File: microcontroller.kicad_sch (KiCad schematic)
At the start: 1 part

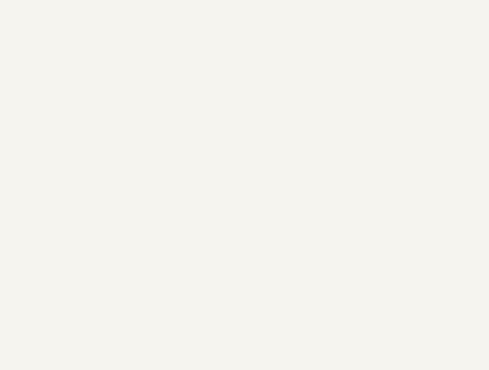
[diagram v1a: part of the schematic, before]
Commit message: added switches
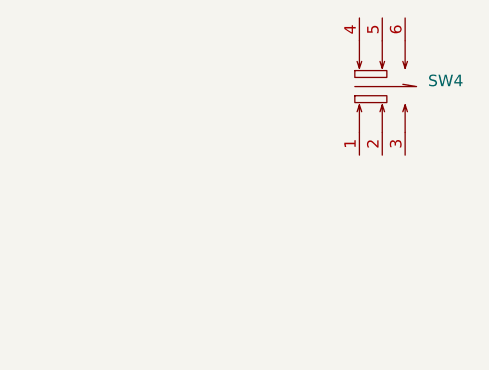
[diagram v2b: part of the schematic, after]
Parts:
- added SW4: ~, Custom_Parts:Switch_XKB5858, symbol Custom_Parts:Switch_XKB5858
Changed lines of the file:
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@@
 	(paper "A4")
+	(symbol
+		(lib_id "Custom_Parts:Switch_XKB5858")
+		(at 222.25 44.45 0)
+		(unit 1)
+		(exclude_from_sim no)
+		(in_bom yes)
+		(on_board yes)
+		(dnp no)
+		(fields_autoplaced yes)
+		(property "Reference" "SW4"
+			(at 227.33 43.8149 0)
+			(effects
+				(font
+					(size 1.27 1.27)
+				)
+				(justify left)
+			)
+		)
+		(property "Value" "~"
+			(at 227.33 45.72 0)
+			(effects
+				(font
+					(size 1.27 1.27)
+				)
+				(justify left)
+			)
+		)
+		(property "Footprint" "Custom_Parts:Switch_XKB5858"
+			(at 222.25 44.45 0)
+			(effects
+				(font
+					(size 1.27 1.27)
+				)
+				(hide yes)
+			)
+		)
+		(property "Datasheet" "https://item.szlcsc.com/datasheet/XKB5858-W-TP-75/724371.html"
+			(at 222.25 44.45 0)
+			(effects
+				(font
+					(size 1.27 1.27)
+				)
+				(hide yes)
+			)
+		)
+		(property "Description" "Self Lock / No Lock:Non-Latching Actuator Style:Square Button Mounting Type:Surface Mount,Vertical Contact Current:100mA Voltage Rating:30V Actuator/Cap Color:White With Lamp:Without Termination Style:SMD(SMT) Tab Operating Force:1.6N Operating Temperatur"
+			(at 222.25 44.45 0)
+			(effects
+				(font
+					(size 1.27 1.27)
+				)
+				(hide yes)
+			)
+		)
+		(property "Manufacturer Part" "XKB5858-W-TP-75"
+			(at 222.25 44.45 0)
+			(effects
+				(font
+					(size 1.27 1.27)
+				)
+				(hide yes)
+			)
+		)
+		(property "Manufacturer" "XKB Connection(中国星坤)"
+			(at 222.25 44.45 0)
+			(effects
+				(font
+					(size 1.27 1.27)
+				)
+				(hide yes)
+			)
+		)
+		(property "Supplier Part" "C692488"
+			(at 222.25 44.45 0)
+			(effects
+				(font
+					(size 1.27 1.27)
+				)
+				(hide yes)
+			)
+		)
+		(property "Supplier" "LCSC"
+			(at 222.25 44.45 0)
+			(effects
+				(font
+					(size 1.27 1.27)
+				)
+				(hide yes)
+			)
+		)
+		(property "LCSC Part Name" "按键开关5.8*按键开关5.8贴片无锁开关 平头"
+			(at 222.25 44.45 0)
+			(effects
+				(font
+					(size 1.27 1.27)
+				)
+				(hide yes)
+			)
+		)
+		(property "LCSC" "C692488"
+			(at 222.25 44.45 0)
+			(effects
+				(font
+					(size 1.27 1.27)
+				)
+				(hide yes)
+			)
+		)
+		(pin "5"
+		)
+		(pin "1"
+		)
+		(pin "6"
+		)
+		(pin "4"
+		)
+		(pin "2"
+		)
+		(pin "3"
+		)
+		(instances
+			(project "mt-rt"
+				(path "/ee47f507-02e8-4ef5-a6d4-1ac4b2022b93/d98c736e-7552-409d-af25-f5fe8dce0887"
+					(reference "SW4")
+					(unit 1)
+				)
+			)
+		)
+	)
 	(symbol
 		(lib_id "MCU_ST_STM32WB:STM32WB55RGVx")

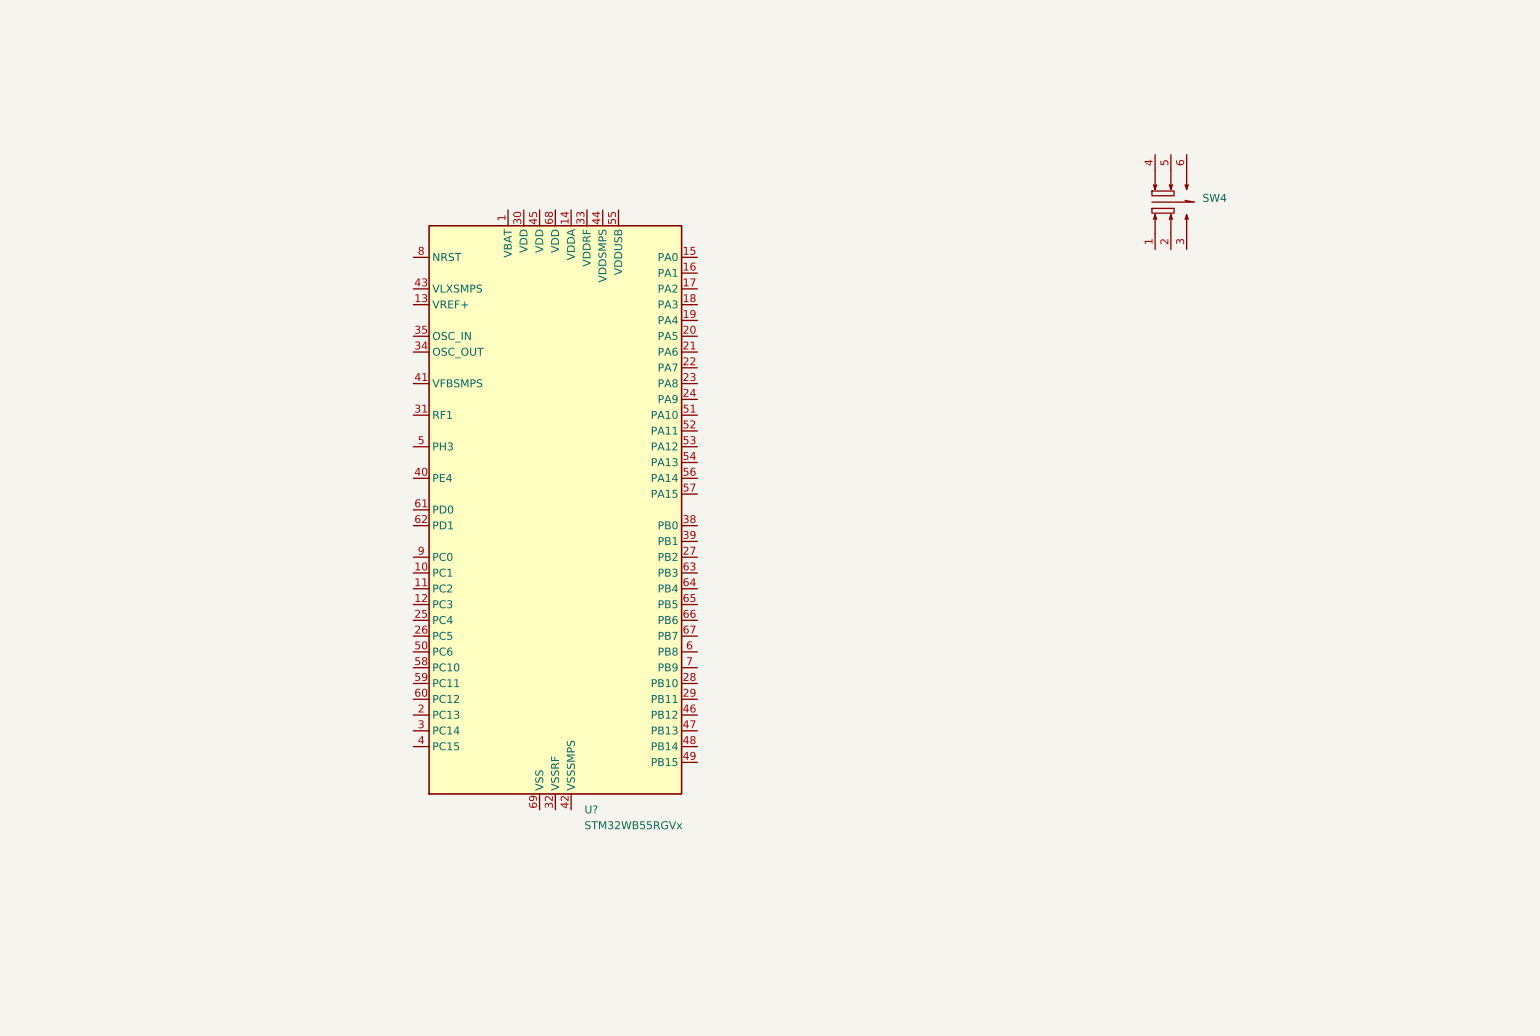
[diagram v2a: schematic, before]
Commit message: Added debug connector and mapped Boot0 and NRST
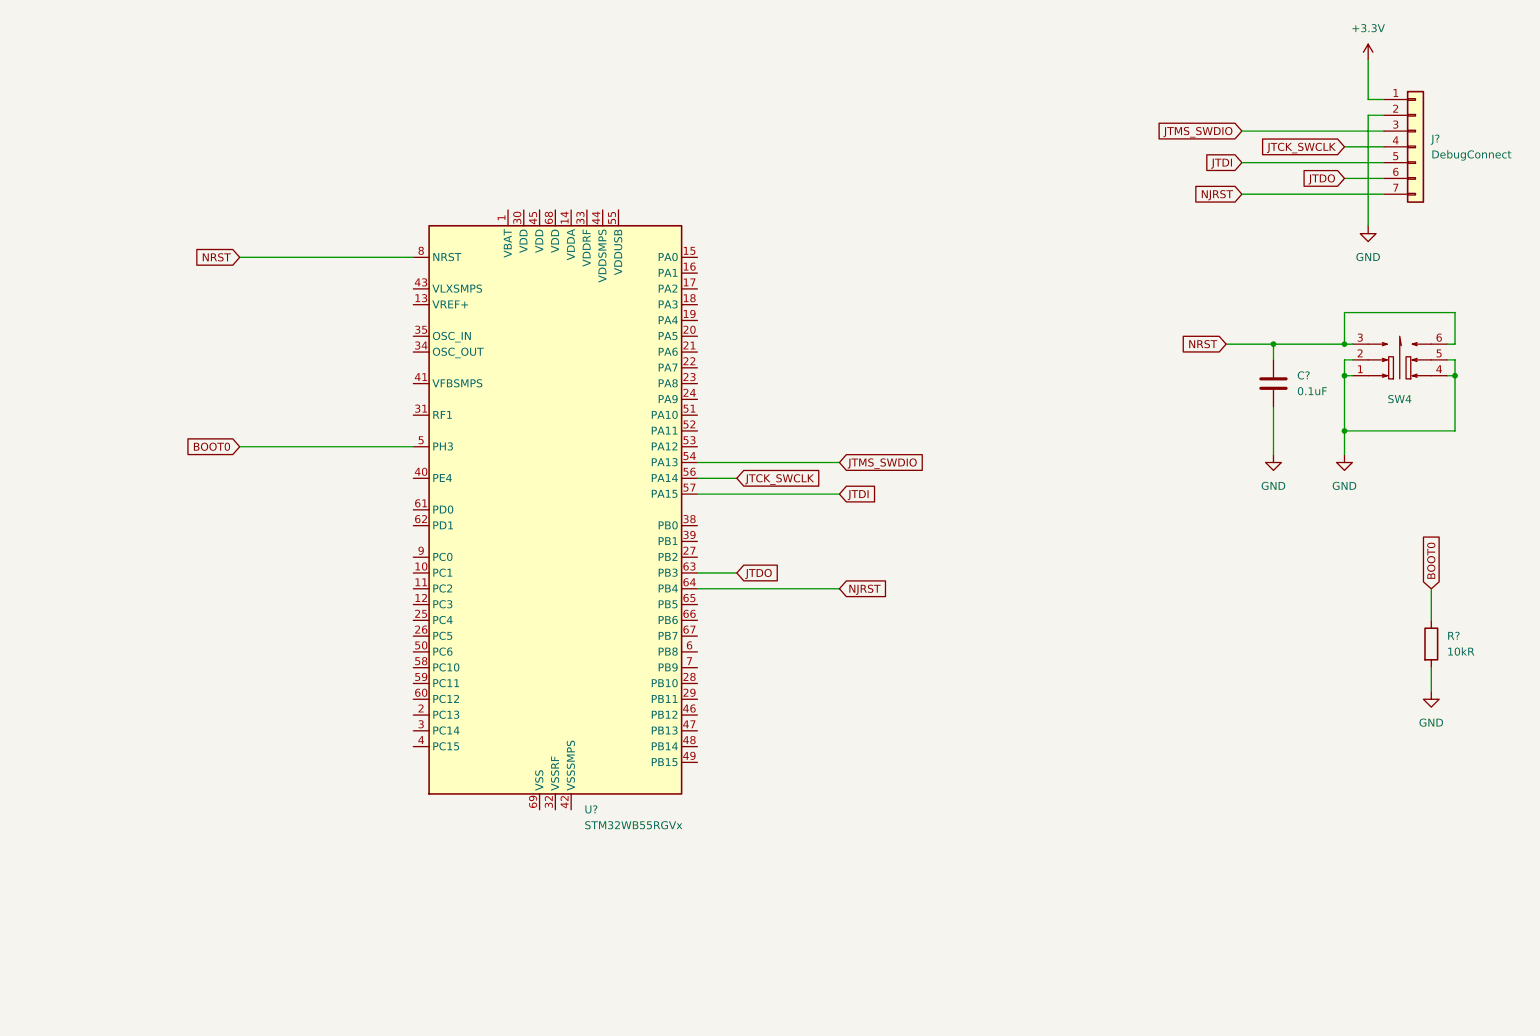
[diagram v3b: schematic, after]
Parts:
- added C?: 0.1uF, Capacitor_SMD:C_0805_2012Metric, symbol Device:C
- added J?: DebugConnect, Connector_PinHeader_2.54mm:PinHeader_1x07_P2.54mm_Vertical, symbol Connector_Generic:Conn_01x07
- added R?: 10kR, Resistor_SMD:R_0805_2012Metric, symbol Device:R
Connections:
- net GND: now reaches SW4.1
- net GND: now also SW4.2, SW4.4, SW4.5, C?.2, J?.2 (Pin_2), R?.2
- net NRST: now reaches SW4.3
- net NRST: now also SW4.6, U?.8 (NRST), C?.1
- net BOOT0: now reaches U?.5 (PH3)
- net BOOT0: now also R?.1
- net JTMS_SWDIO: now reaches U?.54 (PA13)
- net JTMS_SWDIO: now also J?.3 (Pin_3)
- net JTCK_SWCLK: now reaches U?.56 (PA14)
- net JTCK_SWCLK: now also J?.4 (Pin_4)
- net JTDI: now reaches U?.57 (PA15)
- net JTDI: now also J?.5 (Pin_5)
- net JTDO: now reaches U?.63 (PB3)
- net JTDO: now also J?.6 (Pin_6)
- net NJRST: now reaches U?.64 (PB4)
- net NJRST: now also J?.7 (Pin_7)
- new net +3.3V: J?.1 (Pin_1)
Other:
- moved on the sheet: SW4

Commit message: added base VDD Caps added SMPS circuitry added switches MCU added C to reset switch to reduce bouncing
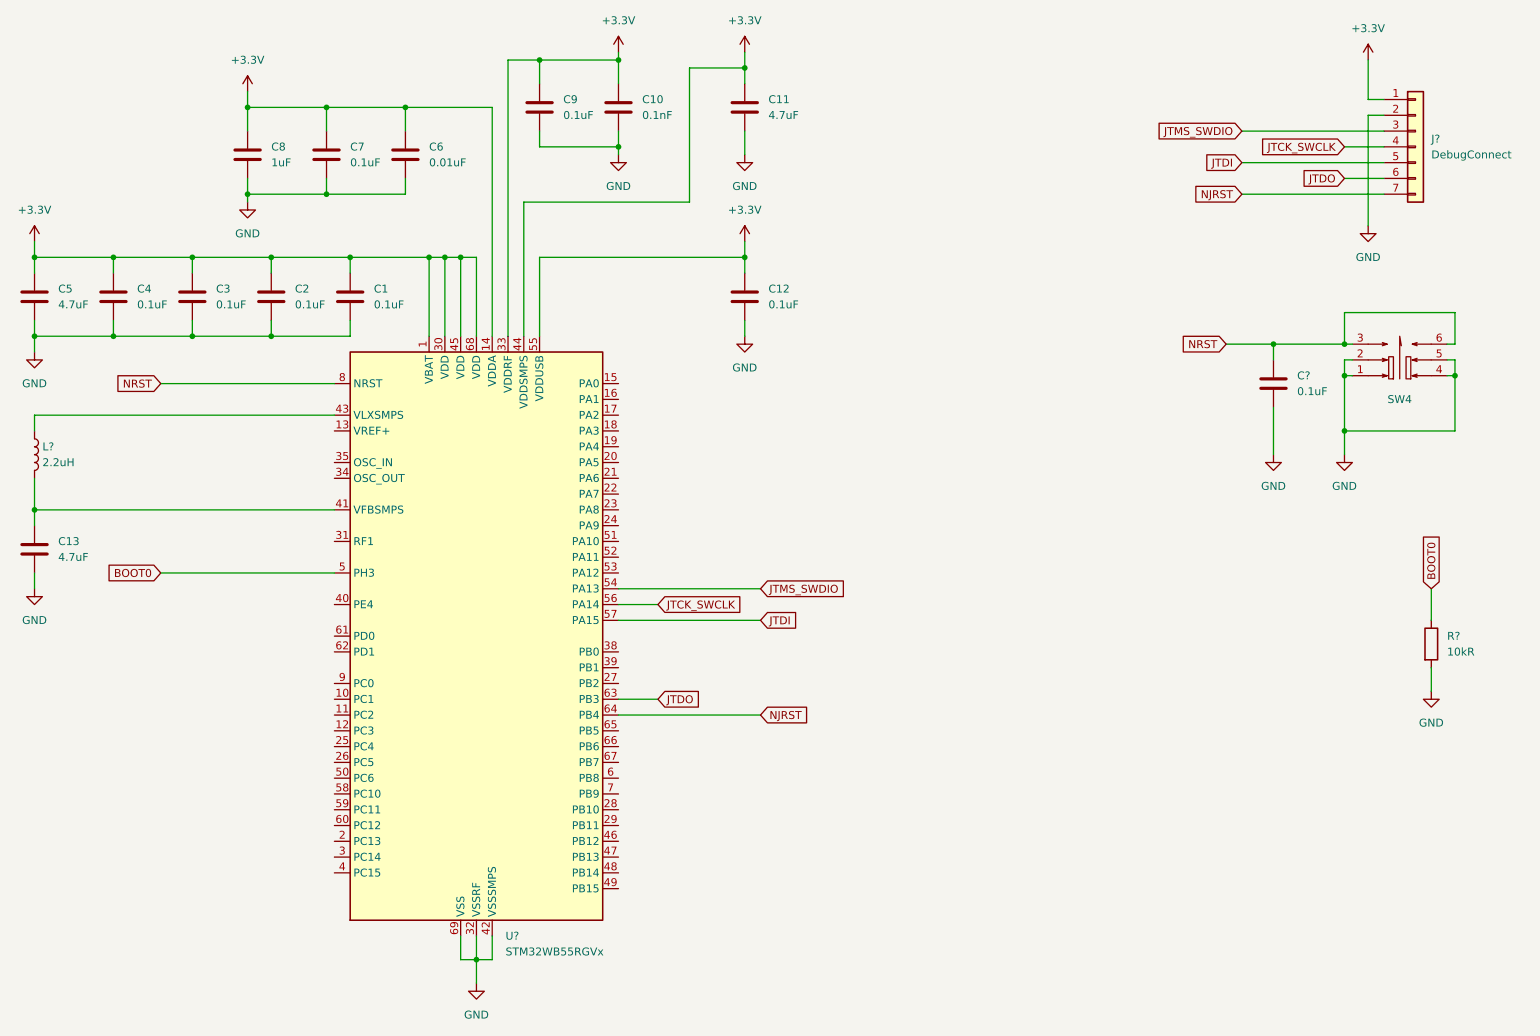
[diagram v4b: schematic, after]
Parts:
- added C1, C12, C2, C3, C4, C7, C9: 0.1uF, Capacitor_SMD:C_0805_2012Metric, symbol Device:C
- added C10: 0.1nF, Capacitor_SMD:C_0805_2012Metric, symbol Device:C
- added C11, C13, C5: 4.7uF, Capacitor_SMD:C_0805_2012Metric, symbol Device:C
- added C6: 0.01uF, Capacitor_SMD:C_0805_2012Metric, symbol Device:C
- added C8: 1uF, Capacitor_SMD:C_0805_2012Metric, symbol Device:C
- added L?: 2.2uH, symbol Device:L
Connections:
- net +3.3V: now also U?.1 (VBAT), U?.14 (VDDA), U?.30 (VDD), U?.33 (VDDRF), U?.44 (VDDSMPS), U?.45 (VDD), U?.55 (VDDUSB), U?.68 (VDD), C1.1, C10.1, C11.1, C12.1, C2.1, C3.1, C4.1, C5.1, C6.1, C7.1, C8.1, C9.1
- net GND: now also U?.32 (VSSRF), U?.42 (VSSSMPS), U?.69 (VSS), C1.2, C10.2, C11.2, C12.2, C13.2, C2.2, C3.2, C4.2, C5.2, C6.2, C7.2, C8.2, C9.2
- net at U?.41 (VFBSMPS): now also C13.1, L?.2
- net at U?.43 (VLXSMPS): now also L?.1
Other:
- moved on the sheet: U?

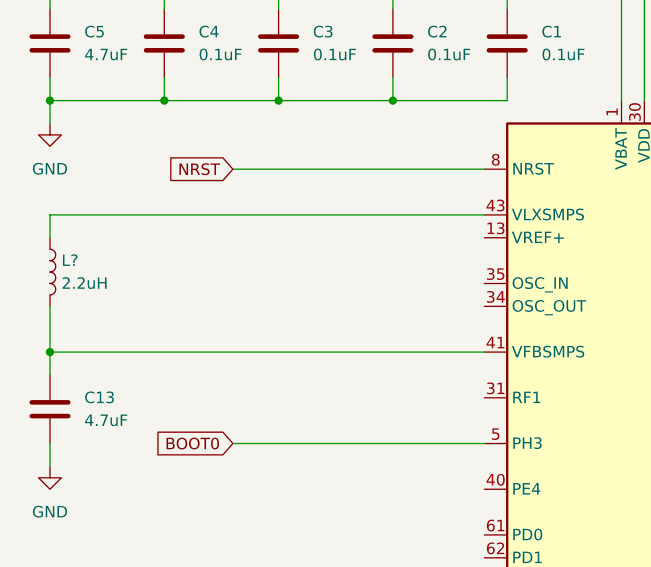
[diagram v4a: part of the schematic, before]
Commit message: changed SMPS operating frequency from 8MHz to a more efficient 4MHz
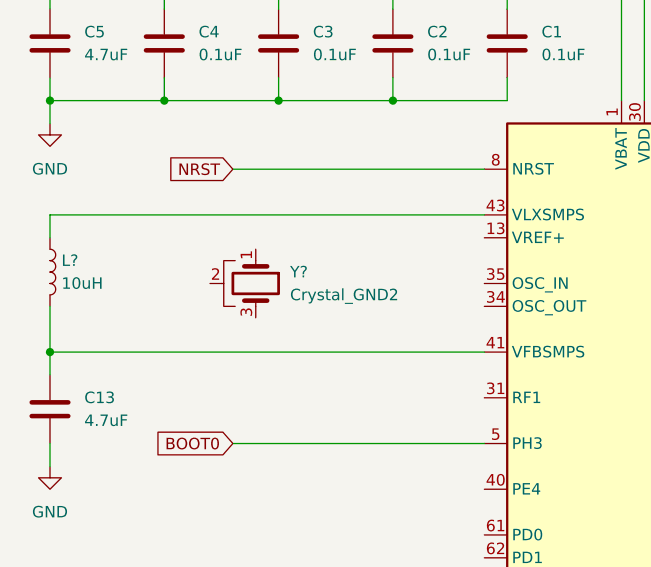
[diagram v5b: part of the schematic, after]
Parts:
- added Y?: Crystal_GND2, symbol Device:Crystal_GND2
- L?: value 2.2uH -> 10uH; footprint (none) -> Custom_Parts:L0805; LSCS C279932 -> C404749
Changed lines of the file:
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@@
 			)
 		)
-		(property "Value" "2.2uH"
+		(property "Value" "10uH"
 			(at 40.64 86.3599 0)
 			(effects
@@
 			)
 		)
-		(property "Footprint" ""
+		(property "Footprint" "Custom_Parts:L0805"
 			(at 39.37 85.09 0)
 			(effects
@@
 			)
 		)
-		(property "LSCS" "C279932"
+		(property "LSCS" "C404749"
 			(at 39.37 85.09 0)
 			(effects
@@
 					(unit 1)
 				)
+			)
+		)
+	)
+	(symbol
+		(lib_id "Device:Crystal_GND2")
+		(at 62.23 86.36 270)
+		(unit 1)
+		(exclude_from_sim no)
+		(in_bom yes)
+		(on_board yes)
+		(dnp no)
+		(fields_autoplaced yes)
+		(property "Reference" "Y?"
+			(at 66.04 85.0899 90)
+			(effects
+				(font
+					(size 1.27 1.27)
+				)
+				(justify left)
+			)
+		)
+		(property "Value" "Crystal_GND2"
+			(at 66.04 87.6299 90)
+			(effects
+				(font
+					(size 1.27 1.27)
+				)
+				(justify left)
+			)
+		)
+		(property "Footprint" ""
+			(at 62.23 86.36 0)
+			(effects
+				(font
+					(size 1.27 1.27)
+				)
+				(hide yes)
+			)
+		)
+		(property "Datasheet" "~"
+			(at 62.23 86.36 0)
+			(effects
+				(font
+					(size 1.27 1.27)
+				)
+				(hide yes)
+			)
+		)
+		(property "Description" "Three pin crystal, GND on pin 2"
+			(at 62.23 86.36 0)
+			(effects
+				(font
+					(size 1.27 1.27)
+				)
+				(hide yes)
+			)
+		)
+		(pin "2"
+		)
+		(pin "1"
+		)
+		(pin "3"
+		)
+		(instances
+			(project ""
+				(path "/ee47f507-02e8-4ef5-a6d4-1ac4b2022b93/d98c736e-7552-409d-af25-f5fe8dce0887"
+					(reference "Y?")
+					(unit 1)
+				)

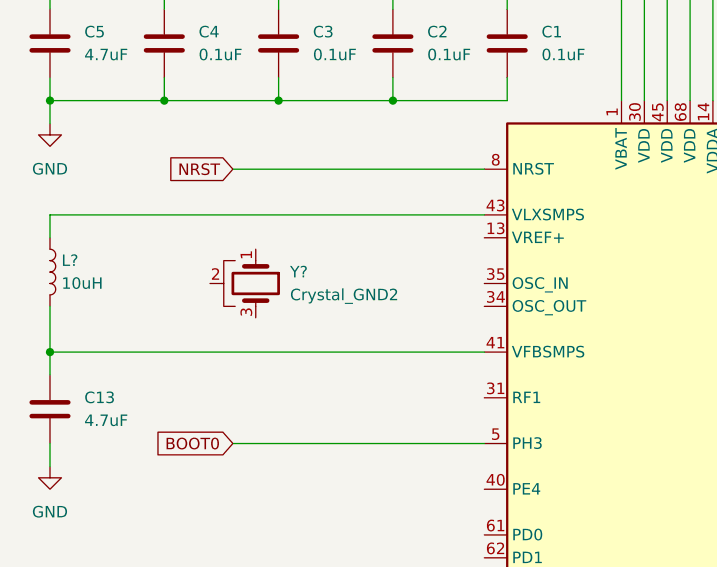
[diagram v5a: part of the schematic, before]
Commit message: added crystal to the MCU
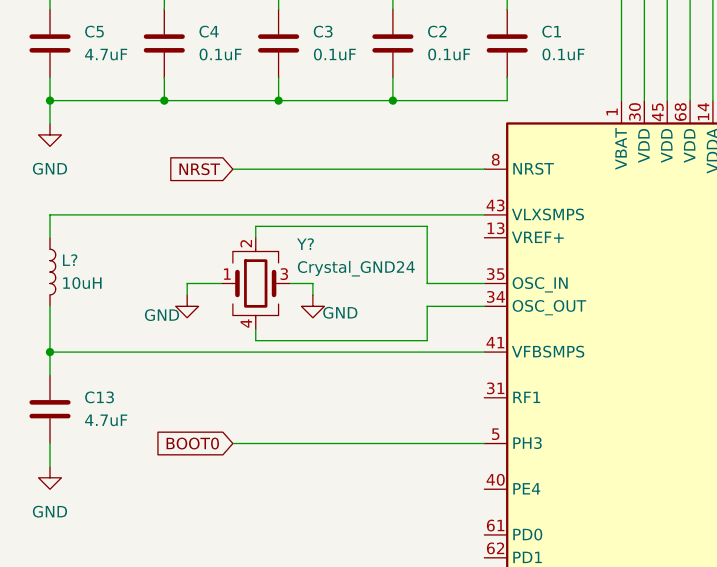
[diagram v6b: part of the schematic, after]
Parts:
- removed Y?: Crystal_GND2, symbol Device:Crystal_GND2
- added Y?: Crystal_GND24, Custom_Parts:CRYSTAL-SMD_4P, symbol Device:Crystal_GND24
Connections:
- net GND: now also Y?.1, Y?.3
- net at U?.34 (OSC_OUT): now also Y?.4
- net at U?.35 (OSC_IN): now also Y?.2

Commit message: annotated full sheet
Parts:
- gave numbers to parts that had none: 6
- renumbered C5 to C1, C9 to C10, C10 to C11, C11 to C12, C12 to C13, C13 to C2, C4 to C3, C3 to C4, C8 to C5, C2 to C6, C1 to C8, C6 to C9, SW4 to SW5
